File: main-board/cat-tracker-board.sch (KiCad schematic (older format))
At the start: 40 parts, among them J1 Conn_01x10, J2 USB_C_Receptacle_USB2.0, J3 Conn_01x03, J4 Conn_01x02, Q1 SI3443DDV-T1-GE3, Q2 Q_PNP_BCE, Q3 Q_NPN_BCE, Q4 SI3443DDV-T1-GE3, Q5 SI3443DDV-T1-GE3, U1 ATSAMD21E18A-A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

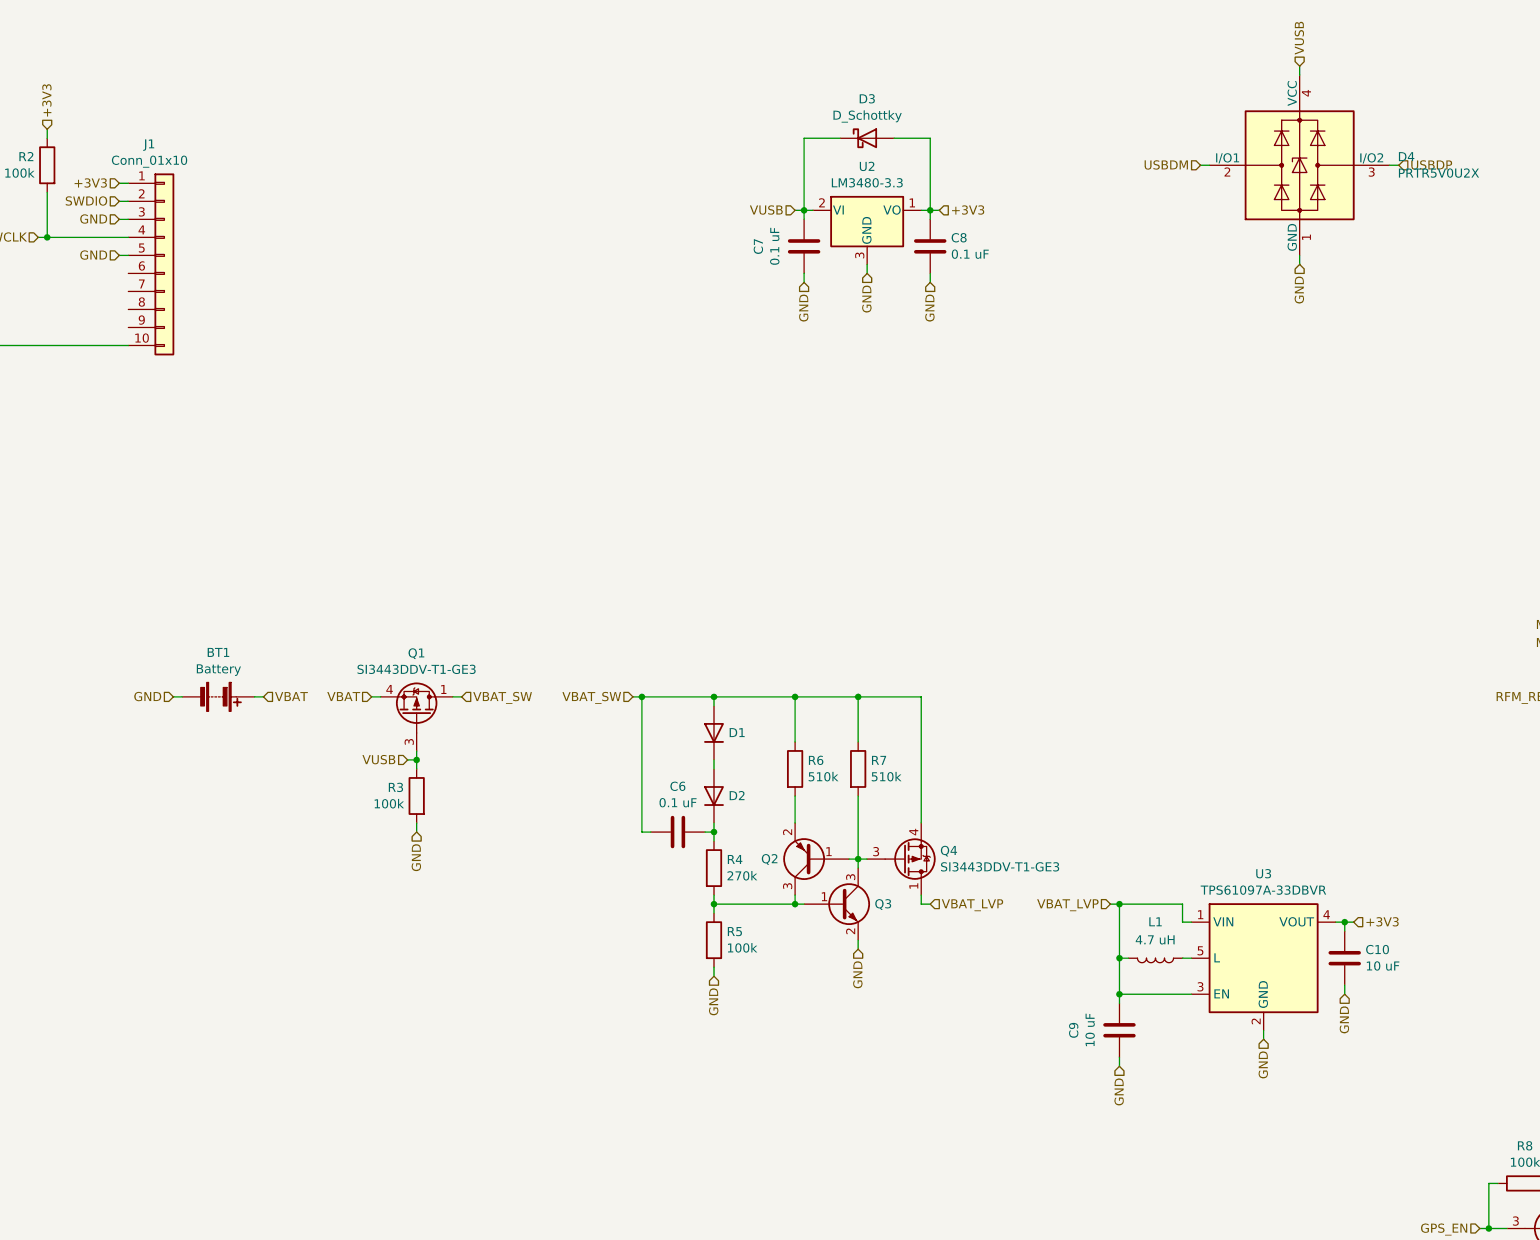
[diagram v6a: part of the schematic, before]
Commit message: Remove LVP circuit and usb/bat selector switch, add slide switch for bat, change switch ind to 10uH.
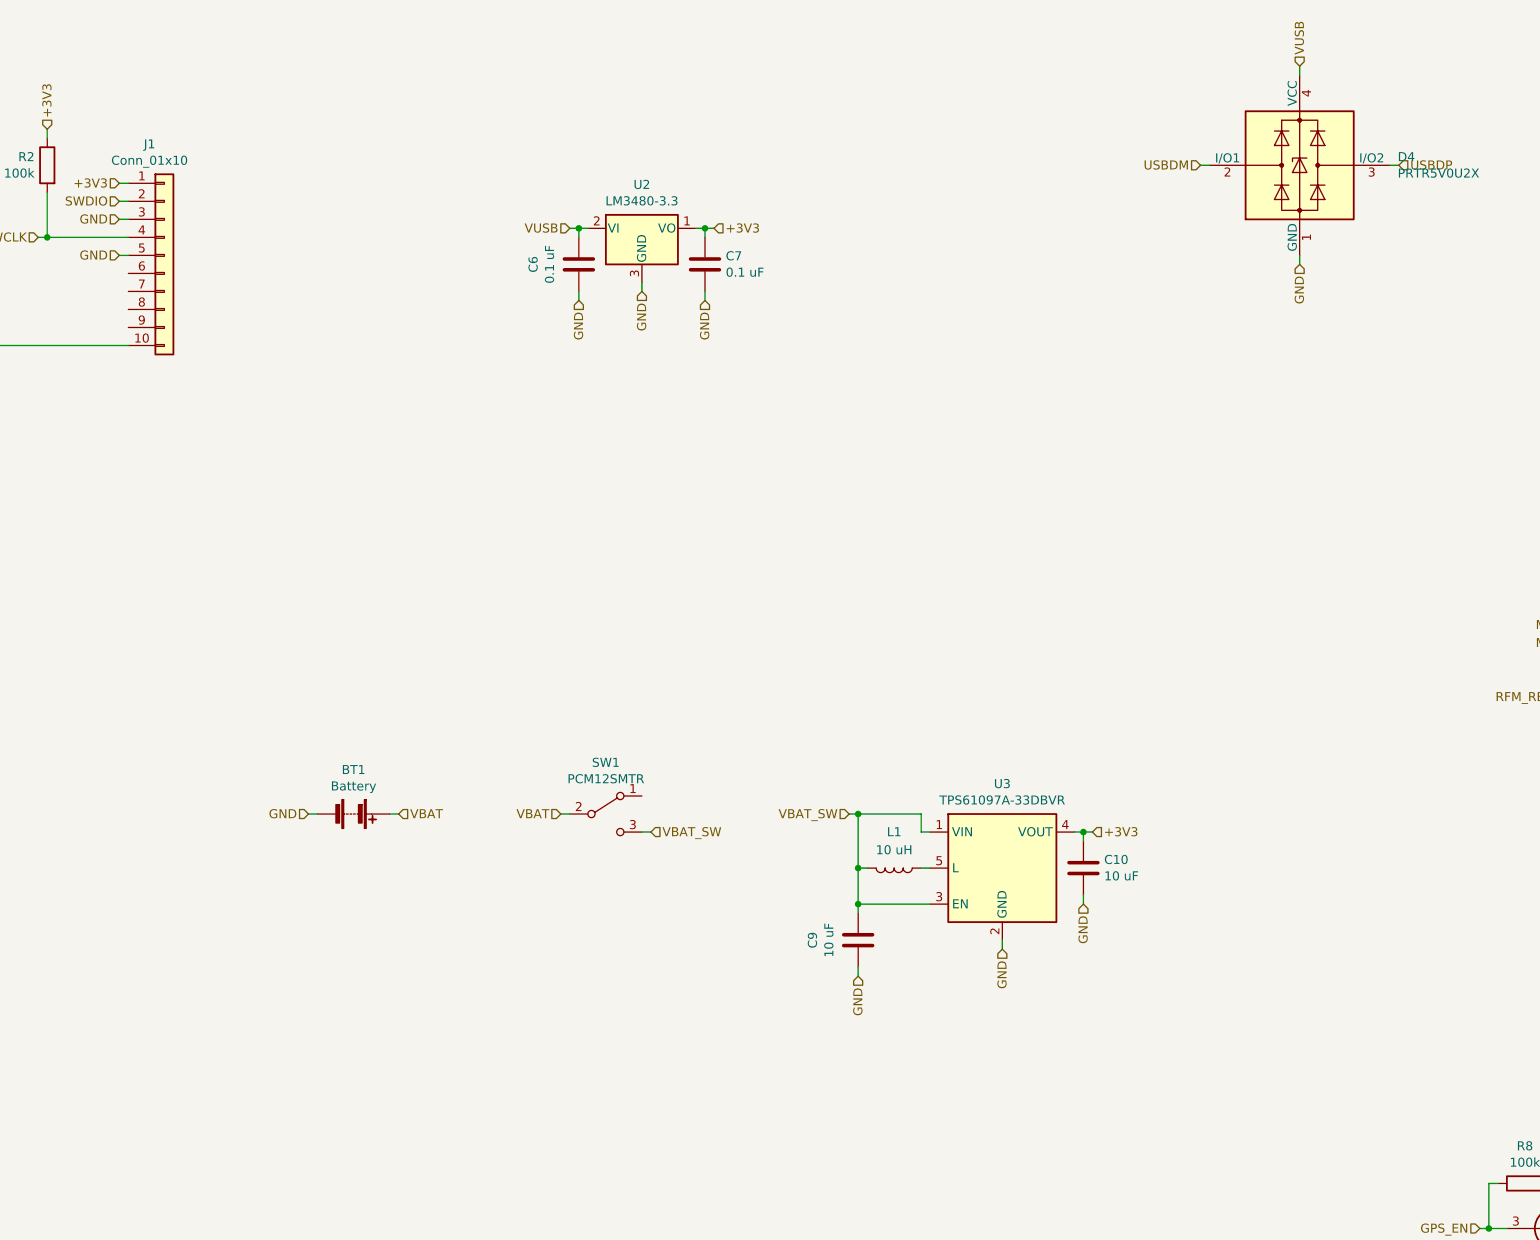
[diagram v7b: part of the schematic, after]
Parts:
- removed C8: 0.1 uF, Capacitor_SMD:C_0805_2012Metric, symbol Device:C
- removed D1, D2: D, Diode_SMD:D_SOD-123, symbol Device:D
- removed D3: D_Schottky, Diode_SMD:D_SOD-123, symbol Device:D_Schottky
- removed Q1, Q4: SI3443DDV-T1-GE3, Package_SO:TSOP-6_1.65x3.05mm_P0.95mm, symbol colinholzman:Si3443
- removed Q2: Q_PNP_BCE, Package_TO_SOT_SMD:SOT-23, symbol Device:Q_PNP_BEC
- removed Q3: Q_NPN_BCE, Package_TO_SOT_SMD:SOT-23, symbol Device:Q_NPN_BEC
- removed R3, R5: 100k, Resistor_SMD:R_0805_2012Metric, symbol Device:R
- removed R4: 270k, Resistor_SMD:R_0805_2012Metric, symbol Device:R
- removed R6, R7: 510k, Resistor_SMD:R_0805_2012Metric, symbol Device:R
- added SW1: PCM12SMTR, Button_Switch_SMD:SW_SPDT_PCM12, symbol Switch:SW_SPDT
- L1: value 4.7 uH -> 10 uH; footprint Inductor_SMD:L_1008_2520Metric -> Inductor_SMD:L_1210_3225Metric; mfg1pn LBC2518T4R7M -> CBC3225T100KR
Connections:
- net VBAT_LVP is gone; now on net VBAT_SW: C9.2, L1.2, U3.1 (VIN), U3.3 (EN)
- net +3V3: now also C7.2
- net GND: now also C6.1
- net VBAT: now also SW1.2 (B)
- net VBAT_SW: now also SW1.3 (C); no longer C6.2
- net VUSB: now also C6.2; no longer C7.2
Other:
- moved on the sheet: BT1, C10, C9, L1, U3

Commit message: Change boost converter inductor to the one used in the reference design.
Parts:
- L1: footprint Inductor_SMD:L_1210_3225Metric -> colinholzman:DO3314-...MLC; mfg1 Taiyo Yuden -> Coilcraft; mfg1pn CBC3225T100KR -> DO3314-103MLC
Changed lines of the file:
@@
 F 0 "L1" V 9350 5700 50  0000 C CNN
 F 1 "10 uH" V 9450 5700 50  0000 C CNN
-F 2 "Inductor_SMD:L_1210_3225Metric" H 9550 5700 50  0001 C CNN
+F 2 "colinholzman:DO3314-...MLC" H 9550 5700 50  0001 C CNN
 F 3 "~" H 9550 5700 50  0001 C CNN
-F 4 "Taiyo Yuden" H 9550 5700 50  0001 C CNN "mfg1"
-F 5 "CBC3225T100KR" H 9550 5700 50  0001 C CNN "mfg1pn"
+F 4 "Coilcraft" H 9550 5700 50  0001 C CNN "mfg1"
+F 5 "DO3314-103MLC" H 9550 5700 50  0001 C CNN "mfg1pn"
 	1    9550 5700
 	0    1    1    0
